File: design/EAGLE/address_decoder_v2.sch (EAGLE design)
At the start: 15 parts, among them IC1 74LS08N, IC10 MC68010P10, IC2 74LS04N, IC3 74LS00N, IC4 74LS21N, IC5 74LS32N, IC6 74LS32N, IC7 74LS02N, IC8 74LS02N, IC9 74LS174N

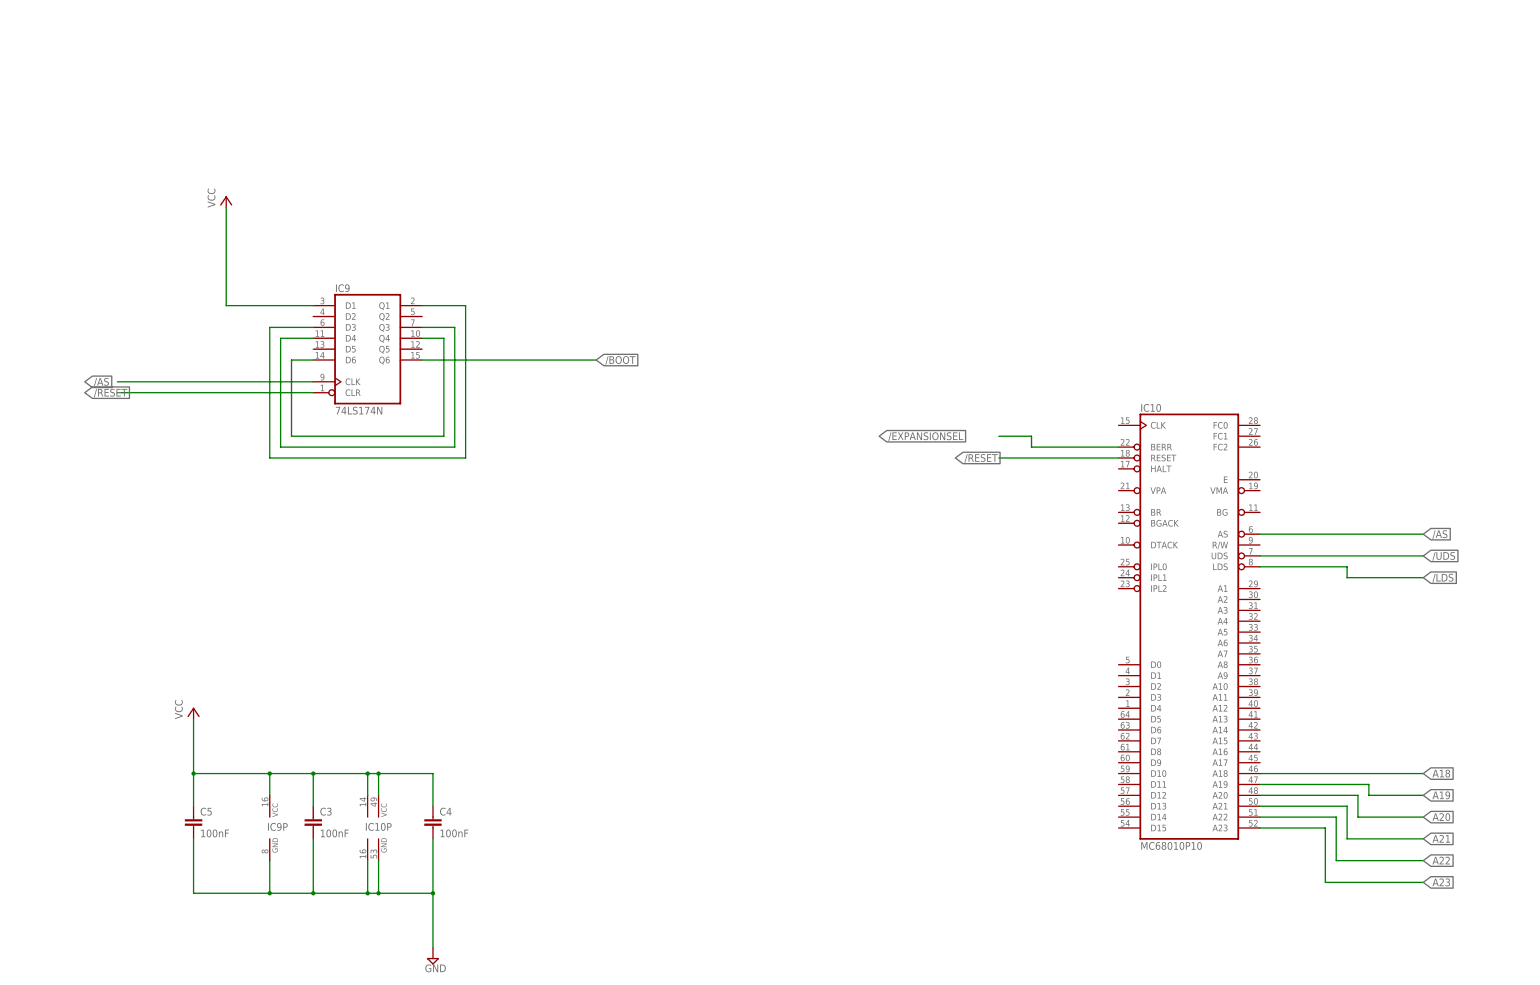
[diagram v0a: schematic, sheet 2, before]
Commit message: Add DTACK generator
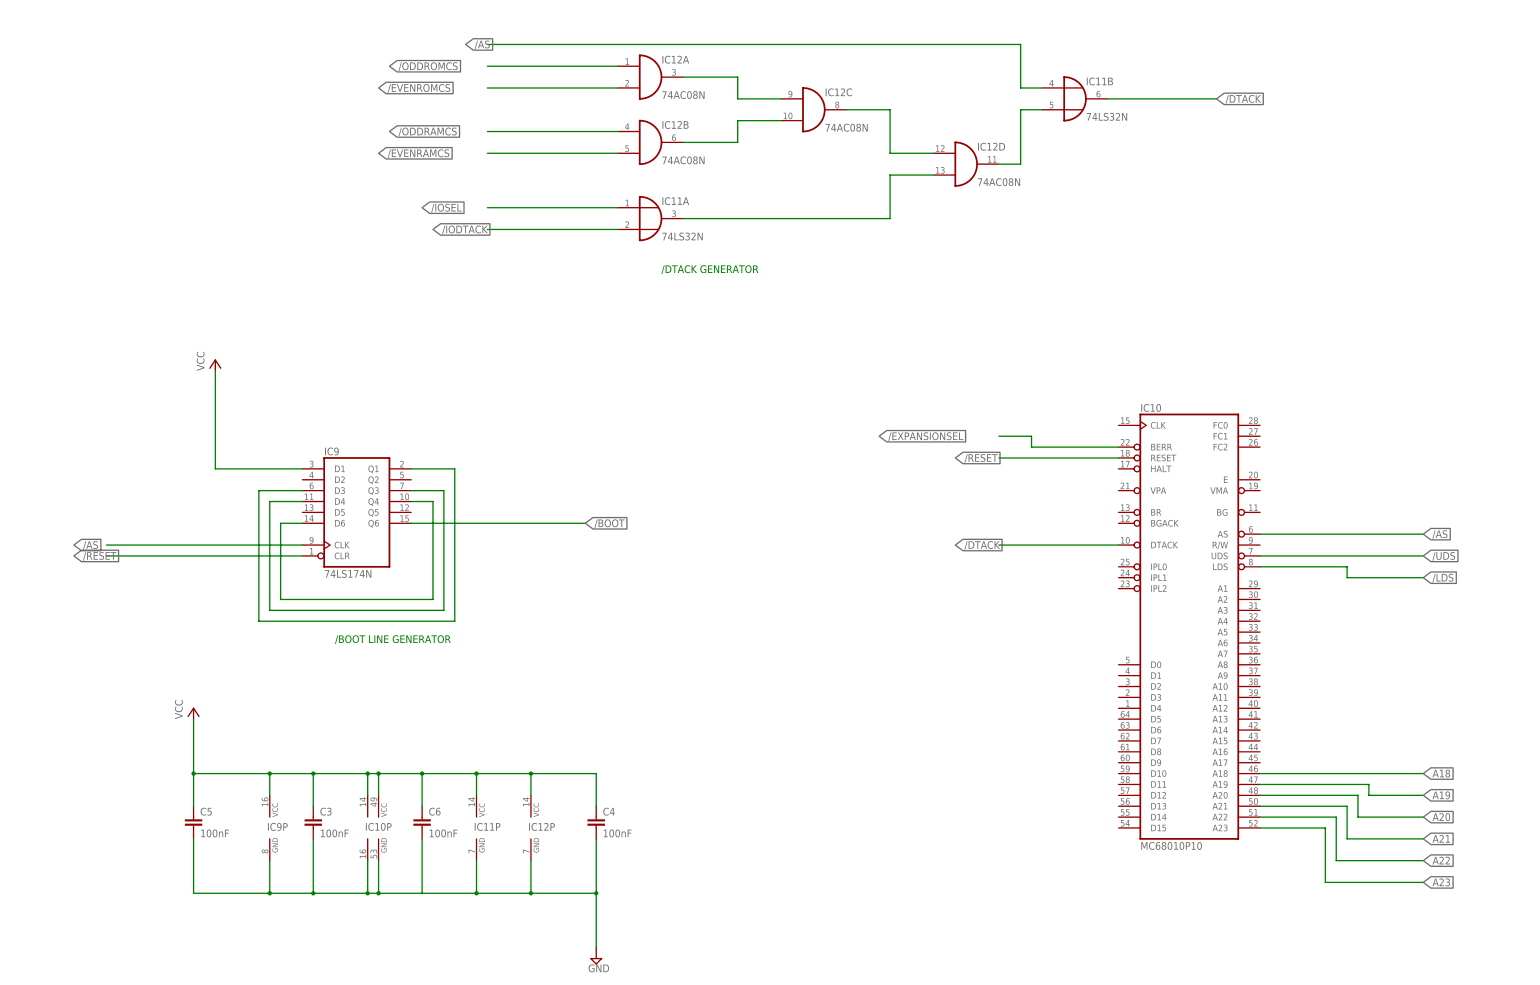
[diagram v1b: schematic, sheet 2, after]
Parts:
- added C6: 100nF, capacitor-wima:C5/3
- added IC11: 74LS32N, 74xx-eu:74LS32N
- added IC12: 74AC08N, 74xx-eu:74AC08N
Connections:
- new net /DTACK: IC10G$1.DTACK, IC11B.O
- new net /IODTACK: IC11A.I1
- new net GND1: C6.2
- new net N$15: IC11B.I1, IC12D.O
- new net N$29: IC12A.O, IC12C.I0
- new net N$30: IC12B.O, IC12C.I1
- new net N$31: IC12C.O, IC12D.I0
- new net N$32: IC11A.O, IC12D.I1
- net /AS: now also IC11B.I0
- net /EVENRAMCS: now also IC12B.I1
- net /EVENROMCS: now also IC12A.I1
- net /IOSEL: now also IC11A.I0
- net /ODDRAMCS: now also IC12B.I0
- net /ODDROMCS: now also IC12A.I0
- net GND: now also IC11P.GND, IC12P.GND
- net VCC: now also C6.1, IC11P.VCC, IC12P.VCC
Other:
- note added: "/BOOT LINE GENERATOR"
- note added: "/DTACK GENERATOR"
- moved on the sheet: C4, IC9

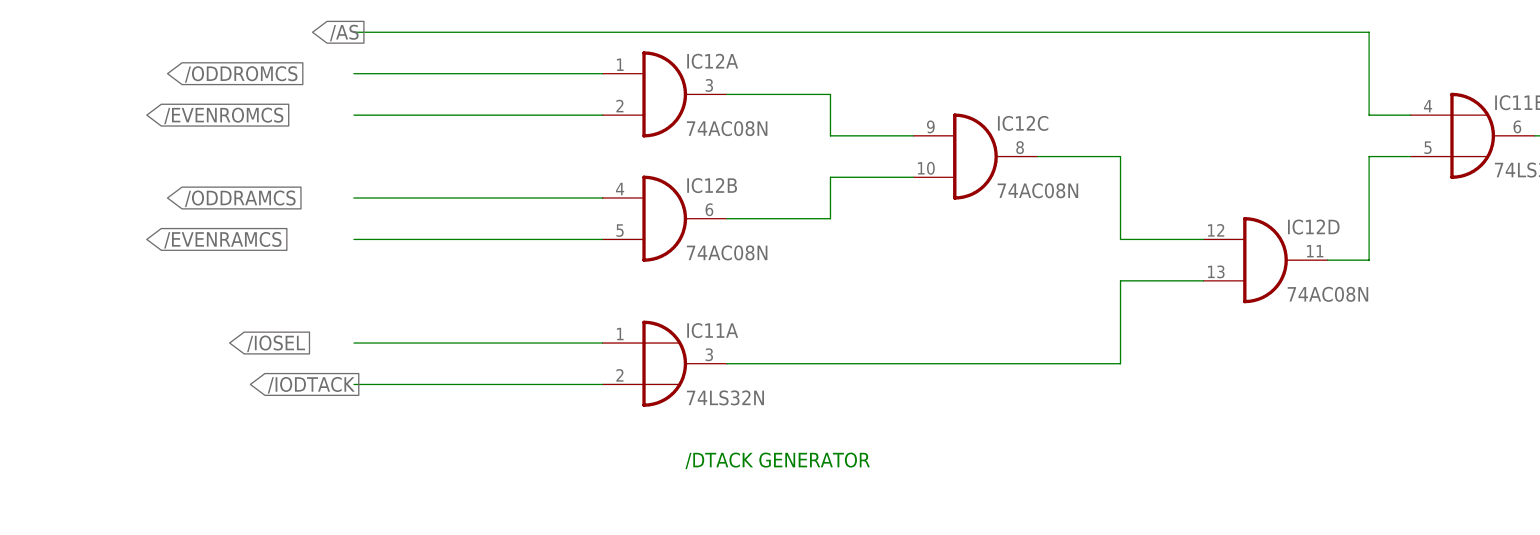
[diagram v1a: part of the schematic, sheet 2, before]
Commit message: New DTACK generator
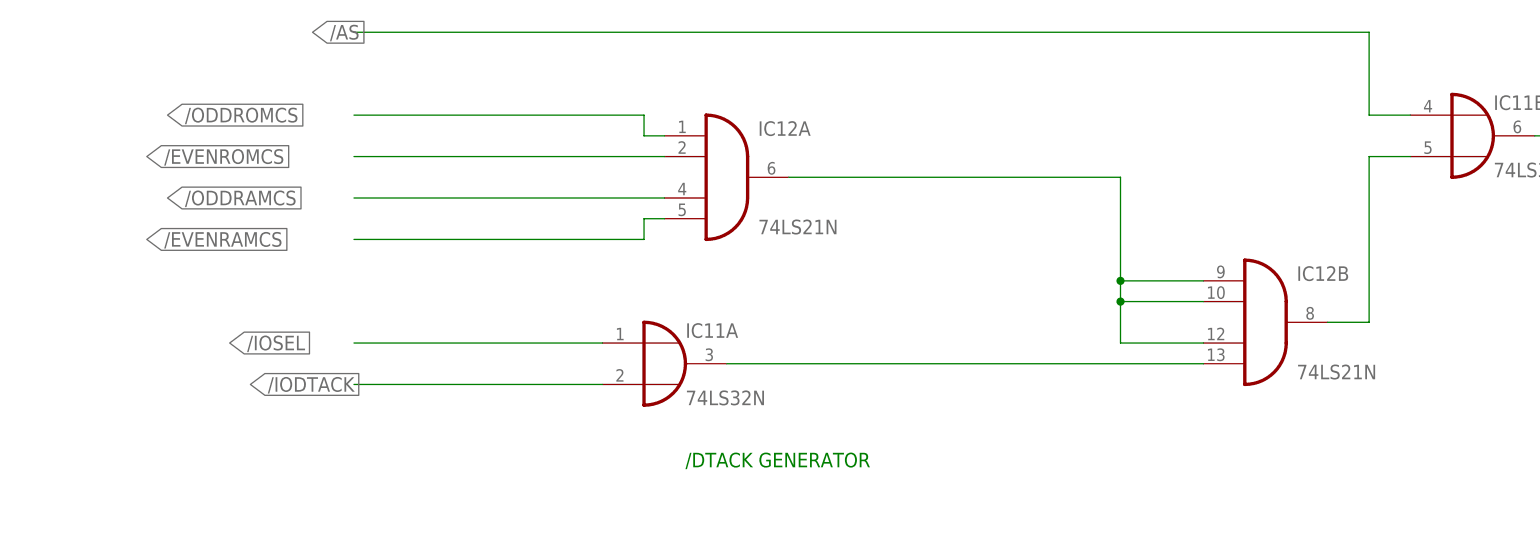
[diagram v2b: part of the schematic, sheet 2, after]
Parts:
- IC12: value 74AC08N -> 74LS21N; device 74xx-eu:74AC08N -> 74xx-eu:74LS21N
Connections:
- removed net N$29: IC12A.O, IC12C.I0
- removed net N$30: IC12B.O, IC12C.I1
- removed net N$31: IC12C.O, IC12D.I0
- new net N$27: IC12A.O, IC12B.I0, IC12B.I1, IC12B.I2
- net /EVENRAMCS: now also IC12A.I3; no longer IC12B.I1
- net /ODDRAMCS: now also IC12A.I2; no longer IC12B.I0
- net N$15: now also IC12B.O; no longer IC12D.O
- net N$32: now also IC12B.I3; no longer IC12D.I1
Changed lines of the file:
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@@
 <part name="SUPPLY2" library="supply2" library_urn="urn:adsk.eagle:library:372" deviceset="GND" device=""/>
 <part name="IC11" library="74xx-eu" library_urn="urn:adsk.eagle:library:85" deviceset="74*32" device="N" package3d_urn="urn:adsk.eagle:package:16407/2" technology="LS"/>
-<part name="IC12" library="74xx-eu" library_urn="urn:adsk.eagle:library:85" deviceset="74*08" device="N" package3d_urn="urn:adsk.eagle:package:16407/2" technology="AC"/>
 <part name="C6" library="capacitor-wima" library_urn="urn:adsk.eagle:library:116" deviceset="C" device="5/3" package3d_urn="urn:adsk.eagle:package:5433/1" value="100nF"/>
+<part name="IC12" library="74xx-eu" library_urn="urn:adsk.eagle:library:85" deviceset="74*21" device="N" package3d_urn="urn:adsk.eagle:package:16407/2" technology="LS"/>
 </parts>
 <sheets>
@@
 <attribute name="VALUE" x="195.58" y="185.42" size="1.778" layer="96"/>
 </instance>
-<instance part="IC12" gate="A" x="193.04" y="223.52" smashed="yes">
-<attribute name="NAME" x="195.58" y="226.695" size="1.778" layer="95"/>
-<attribute name="VALUE" x="195.58" y="218.44" size="1.778" layer="96"/>
-</instance>
-<instance part="IC12" gate="B" x="193.04" y="208.28" smashed="yes">
-<attribute name="NAME" x="195.58" y="211.455" size="1.778" layer="95"/>
-<attribute name="VALUE" x="195.58" y="203.2" size="1.778" layer="96"/>
-</instance>
-<instance part="IC12" gate="C" x="231.14" y="215.9" smashed="yes">
-<attribute name="NAME" x="233.68" y="219.075" size="1.778" layer="95"/>
-<attribute name="VALUE" x="233.68" y="210.82" size="1.778" layer="96"/>
-</instance>
-<instance part="IC12" gate="D" x="266.7" y="203.2" smashed="yes">
-<attribute name="NAME" x="269.24" y="206.375" size="1.778" layer="95"/>
-<attribute name="VALUE" x="269.24" y="198.12" size="1.778" layer="96"/>
-</instance>
 <instance part="IC11" gate="P" x="152.4" y="48.26" smashed="yes">
 <attribute name="NAME" x="151.765" y="47.625" size="1.778" layer="95"/>
-</instance>
-<instance part="IC12" gate="P" x="165.1" y="48.26" smashed="yes">
-<attribute name="NAME" x="164.465" y="47.625" size="1.778" layer="95"/>
 </instance>
 <instance part="C6" gate="G$1" x="139.7" y="50.8" smashed="yes">
@@
 <attribute name="NAME" x="294.64" y="221.615" size="1.778" layer="95"/>
 <attribute name="VALUE" x="294.64" y="213.36" size="1.778" layer="96"/>
+</instance>
+<instance part="IC12" gate="A" x="200.66" y="213.36" smashed="yes">
+<attribute name="NAME" x="204.47" y="218.44" size="1.778" layer="95"/>
+<attribute name="VALUE" x="204.47" y="206.375" size="1.778" layer="96"/>
+</instance>
+<instance part="IC12" gate="B" x="266.7" y="195.58" smashed="yes">
+<attribute name="NAME" x="270.51" y="200.66" size="1.778" layer="95"/>
+<attribute name="VALUE" x="270.51" y="188.595" size="1.778" layer="96"/>
+</instance>
+<instance part="IC12" gate="P" x="165.1" y="48.26" smashed="yes">
+<attribute name="NAME" x="164.465" y="47.625" size="1.778" layer="95"/>
 </instance>
 </instances>
@@
 <wire x1="152.4" y1="55.88" x2="152.4" y2="60.96" width="0.1524" layer="91"/>
 <junction x="152.4" y="60.96"/>
-<pinref part="IC12" gate="P" pin="VCC"/>
 <wire x1="165.1" y1="55.88" x2="165.1" y2="60.96" width="0.1524" layer="91"/>
 <junction x="165.1" y="60.96"/>
+<pinref part="IC12" gate="P" pin="VCC"/>
 </segment>
 </net>
@@
 <wire x1="152.4" y1="40.64" x2="152.4" y2="33.02" width="0.1524" layer="91"/>
 <junction x="152.4" y="33.02"/>
-<pinref part="IC12" gate="P" pin="GND"/>
 <wire x1="165.1" y1="40.64" x2="165.1" y2="33.02" width="0.1524" layer="91"/>
 <junction x="165.1" y="33.02"/>
+<pinref part="IC12" gate="P" pin="GND"/>
 </segment>
 </net>
@@
 <net name="/ODDROMCS" class="0">
 <segment>
+<wire x1="190.5" y1="220.98" x2="154.94" y2="220.98" width="0.1524" layer="91"/>
+<label x="132.08" y="220.98" size="1.778" layer="95" xref="yes"/>
 <pinref part="IC12" gate="A" pin="I0"/>
-<wire x1="185.42" y1="226.06" x2="154.94" y2="226.06" width="0.1524" layer="91"/>
-<label x="132.08" y="226.06" size="1.778" layer="95" xref="yes"/>
+<wire x1="193.04" y1="218.44" x2="190.5" y2="218.44" width="0.1524" layer="91"/>
+<wire x1="190.5" y1="218.44" x2="190.5" y2="220.98" width="0.1524" layer="91"/>
 </segment>
 </net>
 <net name="/EVENROMCS" class="0">
 <segment>
+<wire x1="193.04" y1="215.9" x2="154.94" y2="215.9" width="0.1524" layer="91"/>
+<label x="129.54" y="215.9" size="1.778" layer="95" xref="yes"/>
 <pinref part="IC12" gate="A" pin="I1"/>
-<wire x1="185.42" y1="220.98" x2="154.94" y2="220.98" width="0.1524" layer="91"/>
-<label x="129.54" y="220.98" size="1.778" layer="95" xref="yes"/>
 </segment>
 </net>
 <net name="/ODDRAMCS" class="0">
 <segment>
-<pinref part="IC12" gate="B" pin="I0"/>
-<wire x1="185.42" y1="210.82" x2="154.94" y2="210.82" width="0.1524" layer="91"/>
+<wire x1="193.04" y1="210.82" x2="154.94" y2="210.82" width="0.1524" layer="91"/>
 <label x="132.08" y="210.82" size="1.778" layer="95" xref="yes"/>
+<pinref part="IC12" gate="A" pin="I2"/>
 </segment>
 </net>
 <net name="/EVENRAMCS" class="0">
 <segment>
-<pinref part="IC12" gate="B" pin="I1"/>
-<wire x1="185.42" y1="205.74" x2="154.94" y2="205.74" width="0.1524" layer="91"/>
+<wire x1="190.5" y1="205.74" x2="154.94" y2="205.74" width="0.1524" layer="91"/>
 <label x="129.54" y="205.74" size="1.778" layer="95" xref="yes"/>
+<pinref part="IC12" gate="A" pin="I3"/>
+<wire x1="193.04" y1="208.28" x2="190.5" y2="208.28" width="0.1524" layer="91"/>
+<wire x1="190.5" y1="208.28" x2="190.5" y2="205.74" width="0.1524" layer="91"/>
 </segment>
 </net>
@@
 </segment>
 </net>
-<net name="N$29" class="0">
-<segment>
-<pinref part="IC12" gate="A" pin="O"/>
-<wire x1="200.66" y1="223.52" x2="213.36" y2="223.52" width="0.1524" layer="91"/>
-<wire x1="213.36" y1="223.52" x2="213.36" y2="218.44" width="0.1524" layer="91"/>
-<pinref part="IC12" gate="C" pin="I0"/>
-<wire x1="213.36" y1="218.44" x2="223.52" y2="218.44" width="0.1524" layer="91"/>
-</segment>
-</net>
-<net name="N$30" class="0">
-<segment>
-<pinref part="IC12" gate="B" pin="O"/>
-<wire x1="200.66" y1="208.28" x2="213.36" y2="208.28" width="0.1524" layer="91"/>
-<wire x1="213.36" y1="208.28" x2="213.36" y2="213.36" width="0.1524" layer="91"/>
-<pinref part="IC12" gate="C" pin="I1"/>
-<wire x1="213.36" y1="213.36" x2="223.52" y2="213.36" width="0.1524" layer="91"/>
-</segment>
-</net>
-<net name="N$31" class="0">
-<segment>
-<pinref part="IC12" gate="C" pin="O"/>
-<wire x1="238.76" y1="215.9" x2="248.92" y2="215.9" width="0.1524" layer="91"/>
-<wire x1="248.92" y1="215.9" x2="248.92" y2="205.74" width="0.1524" layer="91"/>
-<pinref part="IC12" gate="D" pin="I0"/>
-<wire x1="248.92" y1="205.74" x2="259.08" y2="205.74" width="0.1524" layer="91"/>
-</segment>
-</net>
 <net name="N$32" class="0">
 <segment>
 <pinref part="IC11" gate="A" pin="O"/>
-<wire x1="200.66" y1="190.5" x2="248.92" y2="190.5" width="0.1524" layer="91"/>
-<wire x1="248.92" y1="190.5" x2="248.92" y2="200.66" width="0.1524" layer="91"/>
-<pinref part="IC12" gate="D" pin="I1"/>
-<wire x1="248.92" y1="200.66" x2="259.08" y2="200.66" width="0.1524" layer="91"/>
+<wire x1="200.66" y1="190.5" x2="259.08" y2="190.5" width="0.1524" layer="91"/>
+<pinref part="IC12" gate="B" pin="I3"/>
 </segment>
 </net>
@@
 <net name="N$15" class="0">
 <segment>
-<pinref part="IC12" gate="D" pin="O"/>
-<wire x1="274.32" y1="203.2" x2="279.4" y2="203.2" width="0.1524" layer="91"/>
-<wire x1="279.4" y1="203.2" x2="279.4" y2="215.9" width="0.1524" layer="91"/>
 <pinref part="IC11" gate="B" pin="I1"/>
 <wire x1="279.4" y1="215.9" x2="284.48" y2="215.9" width="0.1524" layer="91"/>
-</segment>
-</net>
+<wire x1="279.4" y1="215.9" x2="279.4" y2="195.58" width="0.1524" layer="91"/>
+<pinref part="IC12" gate="B" pin="O"/>
+<wire x1="274.32" y1="195.58" x2="279.4" y2="195.58" width="0.1524" layer="91"/>
+</segment>
+</net>
+<net name="N$27" class="0">
+<segment>
+<pinref part="IC12" gate="B" pin="I0"/>
+<pinref part="IC12" gate="B" pin="I1"/>
+<pinref part="IC12" gate="A" pin="O"/>
+<wire x1="208.28" y1="213.36" x2="248.92" y2="213.36" width="0.1524" layer="91"/>
+<pinref part="IC12" gate="B" pin="I2"/>
+<wire x1="248.92" y1="213.36" x2="248.92" y2="200.66" width="0.1524" layer="91"/>
+<wire x1="248.92" y1="200.66" x2="248.92" y2="198.12" width="0.1524" layer="91"/>
+<wire x1="248.92" y1="198.12" x2="248.92" y2="193.04" width="0.1524" layer="91"/>
+<wire x1="248.92" y1="193.04" x2="259.08" y2="193.04" width="0.1524" layer="91"/>
+<wire x1="259.08" y1="198.12" x2="248.92" y2="198.12" width="0.1524" layer="91"/>
+<junction x="248.92" y="198.12"/>
+<wire x1="259.08" y1="200.66" x2="248.92" y2="200.66" width="0.1524" layer="91"/>
+<junction x="248.92" y="200.66"/>
+</segment>
+</net>
